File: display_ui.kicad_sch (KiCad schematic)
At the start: 70 parts, among them SW401 K2-1102SP-C4SC-04, SW402 K2-1102SP-C4SC-04, SW403 K2-1102SP-C4SC-04, SW404 K2-1102SP-C4SC-04, T401 AO3400A, T402 AO3400A, T403 AO3400A, T404 AO3400A, T405 AO3400A, T406 AO3400A, X401 ER-TFT035-6

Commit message: fix power symbol problem.
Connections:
- net GND: now reaches C408.1
- net GND: now also C401.1, C402.1, C403.1, C404.1, C405.1, C406.1, C407.1, C409.1, C410.1, C411.1, D401.2 (C), D402.2 (C), D403.2 (C), D404.2 (C), D405.2 (C), D406.2 (C), D407.2 (C), D408.2 (C), D410.3 (VSS), R402.1, R404.1, R409.1, R411.1, R415.1, R417.1, R421.1, R430.2, R432.2, R435.2, T401.2 (S), T402.2 (S), T403.2 (S), T405.2 (S), T406.2 (S), X401.11 (VSYNC), X401.12 (HSYNC), X401.14 (DE), X401.15 (DB17), X401.16 (DB16), X401.17 (DB15), X401.18 (DB14), X401.19 (DB13), X401.20 (DB12), X401.21 (DB11), X401.22 (DB10), X401.23 (DB9), X401.24 (DB8), X401.25 (DB7), X401.26 (DB6), X401.27 (DB5), X401.28 (DB4), X401.29 (DB3), X401.30 (DB2), X401.31 (DB1), X401.32 (DB0), X401.43 (GND), X401.48 (GND), X401.49 (GND), X401.50 (GND)
- net +3.3V: now reaches C409.2, C410.2, C411.2
- net +3.3V: now also BUZZER401.1 (+), D409.3 (A), D411.1 (K), R401.2, R404.3, R408.2, R411.3, R415.3, R416.2, R420.2, R429.1, R431.1, R434.1, R436.2, T404.1 (G), X401.13 (DOTCLK), X401.35 (RD), X401.40 (VDDI), X401.41 (VDDI), X401.42 (VCI)
- net +5V: now reaches C407.2, D410.1 (VDD)
- net +5V: now also R426.2
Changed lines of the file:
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@@
     (pin "1")
   )
-  (symbol (lib_name "GND_16") (lib_id "eduboardv2:GND") (at 21.59 64.77 0) (unit 1)
+  (symbol (lib_id "eduboardv2:GND") (at 21.59 64.77 0) (unit 1)
     (in_bom yes) (on_board yes) (fields_autoplaced)
     (property "Reference" "#PWR0403" (id 0) (at 21.59 71.12 0)
@@
     (pin "2")
   )
-  (symbol (lib_name "GND_18") (lib_id "eduboardv2:GND") (at 60.96 64.77 0) (unit 1)
+  (symbol (lib_id "eduboardv2:GND") (at 60.96 64.77 0) (unit 1)
     (in_bom yes) (on_board yes) (fields_autoplaced)
     (property "Reference" "#PWR0416" (id 0) (at 60.96 71.12 0)
@@
     (pin "2")
   )
-  (symbol (lib_name "GND_12") (lib_id "eduboardv2:GND") (at 35.56 165.1 0) (unit 1)
+  (symbol (lib_id "eduboardv2:GND") (at 35.56 165.1 0) (unit 1)
     (in_bom yes) (on_board yes) (fields_autoplaced)
     (property "Reference" "#PWR0408" (id 0) (at 35.56 171.45 0)
@@
     (pin "2")
   )
-  (symbol (lib_name "GND_13") (lib_id "eduboardv2:GND") (at 45.72 64.77 0) (unit 1)
+  (symbol (lib_id "eduboardv2:GND") (at 45.72 64.77 0) (unit 1)
     (in_bom yes) (on_board yes) (fields_autoplaced)
     (property "Reference" "#PWR0410" (id 0) (at 45.72 71.12 0)
@@
     (pin "2")
   )
-  (symbol (lib_name "GND_19") (lib_id "eduboardv2:GND") (at 68.58 64.77 0) (unit 1)
+  (symbol (lib_id "eduboardv2:GND") (at 68.58 64.77 0) (unit 1)
     (in_bom yes) (on_board yes) (fields_autoplaced)
     (property "Reference" "#PWR0419" (id 0) (at 68.58 71.12 0)
@@
     (pin "3")
   )
-  (symbol (lib_name "GND_11") (lib_id "eduboardv2:GND") (at 20.32 167.64 0) (unit 1)
+  (symbol (lib_id "eduboardv2:GND") (at 20.32 167.64 0) (unit 1)
     (in_bom yes) (on_board yes) (fields_autoplaced)
     (property "Reference" "#PWR0402" (id 0) (at 20.32 173.99 0)
@@
     (pin "1")
   )
-  (symbol (lib_name "+3.3V_13") (lib_id "eduboardv2:+3.3V") (at 162.56 87.63 0) (unit 1)
+  (symbol (lib_name "+3.3V_15") (lib_id "eduboardv2:+3.3V") (at 162.56 87.63 0) (unit 1)
     (in_bom yes) (on_board yes) (fields_autoplaced)
     (property "Reference" "#PWR0438" (id 0) (at 162.56 91.44 0)
@@
     (pin "2")
   )
-  (symbol (lib_name "+5V_1") (lib_id "eduboardv2:+5V") (at 123.19 92.71 0) (unit 1)
+  (symbol (lib_id "eduboardv2:+5V") (at 123.19 92.71 0) (unit 1)
     (in_bom yes) (on_board yes) (fields_autoplaced)
     (property "Reference" "#PWR0433" (id 0) (at 123.19 96.52 0)
@@
     (pin "1")
   )
-  (symbol (lib_name "GND_17") (lib_id "eduboardv2:GND") (at 53.34 64.77 0) (unit 1)
+  (symbol (lib_id "eduboardv2:GND") (at 53.34 64.77 0) (unit 1)
     (in_bom yes) (on_board yes) (fields_autoplaced)
     (property "Reference" "#PWR0413" (id 0) (at 53.34 71.12 0)
@@
     (pin "2")
   )
-  (symbol (lib_name "GND_15") (lib_id "eduboardv2:GND") (at 30.48 64.77 0) (unit 1)
+  (symbol (lib_id "eduboardv2:GND") (at 30.48 64.77 0) (unit 1)
     (in_bom yes) (on_board yes) (fields_autoplaced)
     (property "Reference" "#PWR0406" (id 0) (at 30.48 71.12 0)
@@
     (pin "2")
   )
-  (symbol (lib_name "+5V_1") (lib_id "eduboardv2:+5V") (at 157.48 82.55 0) (unit 1)
+  (symbol (lib_id "eduboardv2:+5V") (at 157.48 82.55 0) (unit 1)
     (in_bom yes) (on_board yes) (fields_autoplaced)
     (property "Reference" "#PWR0437" (id 0) (at 157.48 86.36 0)
@@
     (pin "2")
   )
-  (symbol (lib_name "GND_32") (lib_id "eduboardv2:GND") (at 53.34 102.87 0) (unit 1)
+  (symbol (lib_id "eduboardv2:GND") (at 53.34 102.87 0) (unit 1)
     (in_bom yes) (on_board yes) (fields_autoplaced)
     (property "Reference" "#PWR0415" (id 0) (at 53.34 109.22 0)
@@
     (pin "3")
   )
-  (symbol (lib_name "GND_14") (lib_id "eduboardv2:GND") (at 38.1 64.77 0) (unit 1)
+  (symbol (lib_id "eduboardv2:GND") (at 38.1 64.77 0) (unit 1)
     (in_bom yes) (on_board yes) (fields_autoplaced)
     (property "Reference" "#PWR0409" (id 0) (at 38.1 71.12 0)

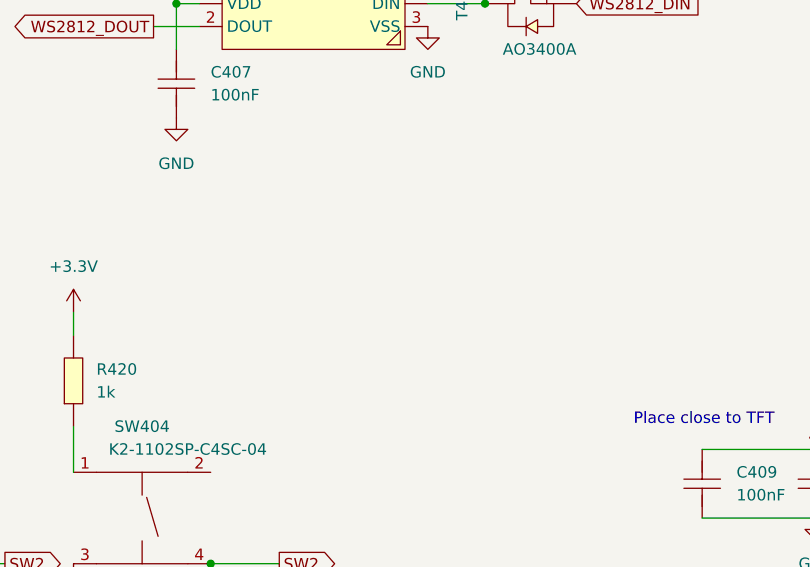
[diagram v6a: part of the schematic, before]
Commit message: added rotary encoder
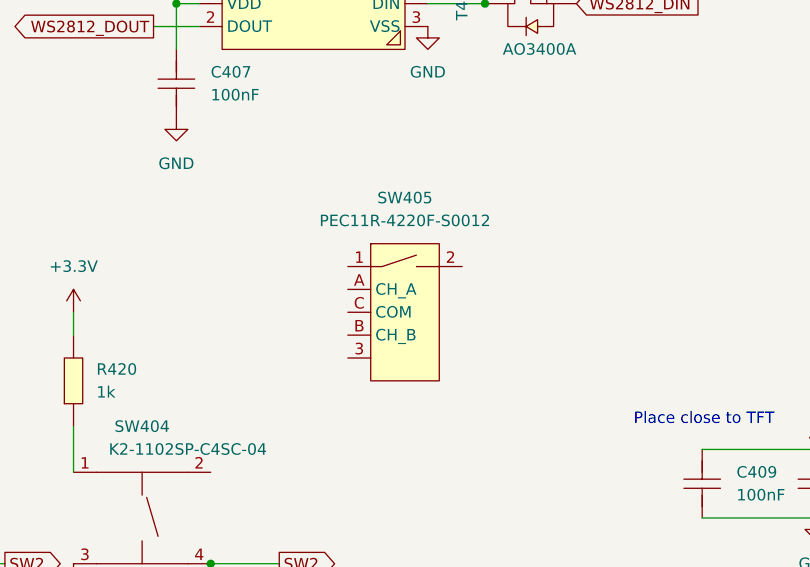
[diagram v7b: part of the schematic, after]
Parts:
- added SW405: PEC11R-4220F-S0012, SW-TH_PEC11R-4220F-S0012, symbol eduboardv2:PEC11R-4220F-S0012
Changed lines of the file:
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@@
     (pin "2")
+  )
+  (symbol (lib_id "eduboardv2:PEC11R-4220F-S0012") (at 148.59 129.54 0) (unit 1)
+    (in_bom yes) (on_board yes) (fields_autoplaced)
+    (property "Reference" "SW405" (id 0) (at 148.59 116.84 0))
+    (property "Value" "PEC11R-4220F-S0012" (id 1) (at 148.59 119.38 0))
+    (property "Footprint" "SW-TH_PEC11R-4220F-S0012" (id 2) (at 148.59 142.24 0)
+      (effects (font (size 1.27 1.27)) hide)
+    )
+    (property "Datasheet" "https://lcsc.com/product-detail/Coded-Rotary-Switches_BOURNS_PEC11R-4220F-S0012_PEC11R-4220F-S0012_C143817.html" (id 3) (at 148.59 147.32 0)
+      (effects (font (size 1.27 1.27)) hide)
+    )
+    (property "Manufacturer" "BOURNS" (id 4) (at 148.59 149.86 0)
+      (effects (font (size 1.27 1.27)) hide)
+    )
+    (property "LCSC Part" "C143817" (id 5) (at 148.59 152.4 0)
+      (effects (font (size 1.27 1.27)) hide)
+    )
+    (property "JLC Part" "Extended Part" (id 6) (at 148.59 154.94 0)
+      (effects (font (size 1.27 1.27)) hide)
+    )
+    (property "MPN" "PEC11R-4220F-S0012" (id 7) (at 148.59 139.7 0)
+      (effects (font (size 1.27 1.27)) hide)
+    )
+    (pin "1")
+    (pin "2")
+    (pin "3")
+    (pin "A")
+    (pin "B")
+    (pin "C")
   )
   (symbol (lib_id "eduboardv2:MLT-8530") (at 179.07 25.4 0) (unit 1)

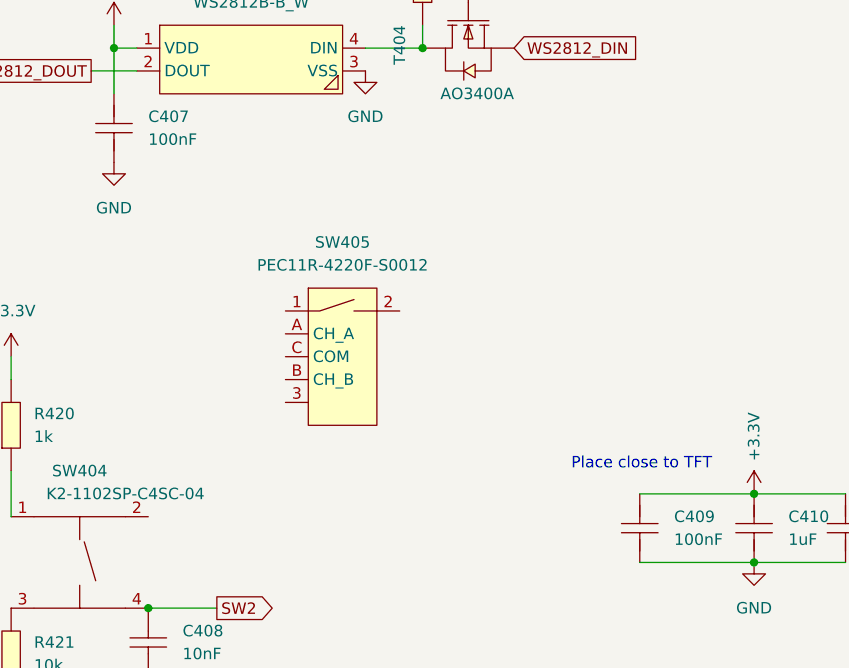
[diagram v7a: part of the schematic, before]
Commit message: add rotary encoder circuit
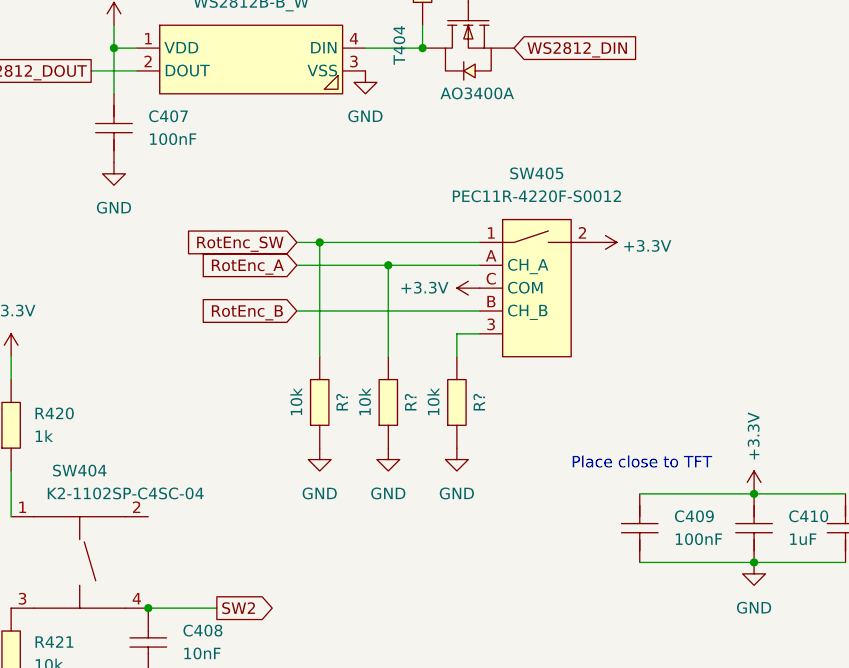
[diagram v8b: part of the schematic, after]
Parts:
- added R? (x3): 10k, eduboardv2:R0402, symbol eduboardv2:0402WGF100JTCE
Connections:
- net +3.3V: now also SW405.2, SW405.C (COM)
- net GND: now also R?.1, R?.1, R?.1
- net RotEnc_SW: now reaches SW405.1
- net RotEnc_SW: now also R?.2
- net at SW405.3: now also R?.2
- net RotEnc_A: now reaches SW405.A (CH_A)
- net RotEnc_A: now also R?.2
- net RotEnc_B: now reaches SW405.B (CH_B)
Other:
- moved on the sheet: SW405
